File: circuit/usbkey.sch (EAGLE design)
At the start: 29 parts, among them IC1 ATmega168P, Q1 16MHz, X1 1503_09, X2 USB

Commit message: update
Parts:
- removed C5: 1u, resistor:C-US025-024X044
- removed C6: 0.1u, resistor:C-US025-024X044
- removed JP1: AVR-ISP-6VERT, avr-7:AVR-ISP-6VERT
- removed JP3: (no value), pinhead:PINHD-1X9
- removed R5: VARISTOR, varistor:VARISTOR-2,5
- removed R9: 1k, resistor:R-US_0204/7
- removed SPEAKER: (no value), pinhead:PINHD-1X2
- added D3, D4: 5V, diode:BZX55
- added P1: SPEAKER, pinhead:PINHD-1X2
- added PISP: AVR-ISP-6VERT, avr-7:AVR-ISP-6VERT
- C1, C2: value 0.1u -> 22p; device resistor:C-US025-024X044 -> c-j:C-50V-0302-2.54
- C3: device resistor:C-US025-024X044 -> c-j:C-50V-0302-2.54
- C4: value 1u -> 0.1u; device resistor:C-US025-024X044 -> c-j:C-50V-0302-2.54
- LED1: value (none) -> MONITOR
- P2: value (none) -> LED
- P3: value (none) -> OUTPUT
- R1, R2: value 168 -> 68; device resistor:R-US_0204/2V -> r-j:R-1/4W-07.62
- R3: device resistor:R-US_0204/7 -> r-j:R-1/4W-02.54-V
- R4: value VARISTOR -> 1.5k; device varistor:VARISTOR-2,5 -> r-j:R-1/4W-02.54-V
- R6: device resistor:R-US_0204/2V -> r-j:R-1/4W-02.54-V
- R7: device resistor:R-US_0204/2V -> r-j:R-1/4W-07.62
- R8: device resistor:R-US_0204/7 -> r-j:R-1/4W-07.62
- renumbered LED to P2, OUTPUT to P3
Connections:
- removed net N$20: C4.1, JP3.2
- removed net N$21: C5.1, JP3.4
- removed net N$22: C5.2, JP3.3
- removed net N$23: IC1.PC4(ADC4/SDA), JP3.7, R8.1
- removed net N$24: IC1.PC5(ADC5/SCL), JP3.8, R9.1
- net GND: now also C4.1, D3.A, D4.A, P1.2, PISP.6; no longer C6.2, JP1.6, JP3.6, R4.2, R5.2, SPEAKER.2
- net N$10: now also PISP.4; no longer JP1.4
- net N$11: now also PISP.3; no longer JP1.3
- net N$12: now also PISP.1; no longer JP1.1
- net N$14: now also P1.1; no longer SPEAKER.1
- net N$7: now also D3.C; no longer R4.1
- net N$8: now also D4.C; no longer R5.1
- net N$9: now also C4.2, PISP.5, R4.1; no longer JP1.5
- net VCC: now also IC1.AVCC, PISP.2, R4.2; no longer C4.2, C6.1, JP1.2, JP3.5, JP3.9, R8.2, R9.2
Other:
- moved on the sheet: SG1, X1

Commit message: update
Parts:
- removed R8: 1k, r-j:R-1/4W-07.62
- added C5, C6: 100p, c-j:C-50V-0302-2.54
- added JP1: (no value), pinhead:PINHD-1X3
- added JP2: (no value), pinhead:PINHD-1X6
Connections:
- new net N$20: IC1.PC0(ADC0), JP2.1
- new net N$21: IC1.PC1(ADC1), JP2.2
- new net N$22: IC1.PC2(ADC2), JP2.3
- new net N$23: IC1.PC3(ADC3), JP2.4
- new net N$24: IC1.PC4(ADC4/SDA), JP2.5
- new net N$25: IC1.PC5(ADC5/SCL), JP2.6
- net GND: now also C5.2, C6.2, JP1.1; no longer X1.1
- net N$3: now also C5.1
- net N$5: now also C6.1
- net N$7: now also JP1.3; no longer X1.3
- net N$8: now also JP1.2; no longer X1.2
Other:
- moved on the sheet: D3, D4, X1

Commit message: update
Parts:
- added C7: 0.1u, c-j:C-50V-0302-2.54
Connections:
- net GND: now also C7.1
- net VCC: now also C7.2
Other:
- moved on the sheet: LED1, OK1, P1, P2, P3, PISP, R6, R7, SG1

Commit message: update
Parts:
- R3: device r-j:R-1/4W-02.54-V -> r-j:R-1/4W-07.62
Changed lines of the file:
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@@
 <part name="R1" library="r-j" deviceset="R-" device="1/4W-07.62" value="68"/>
 <part name="R2" library="r-j" deviceset="R-" device="1/4W-07.62" value="68"/>
-<part name="R3" library="r-j" deviceset="R-" device="1/4W-02.54-V" value="1.5k"/>
+<part name="R3" library="r-j" deviceset="R-" device="1/4W-07.62" value="1.5k"/>
 <part name="GND3" library="supply1" deviceset="GND" device=""/>
 <part name="R6" library="r-j" deviceset="R-" device="1/4W-02.54-V" value="100"/>

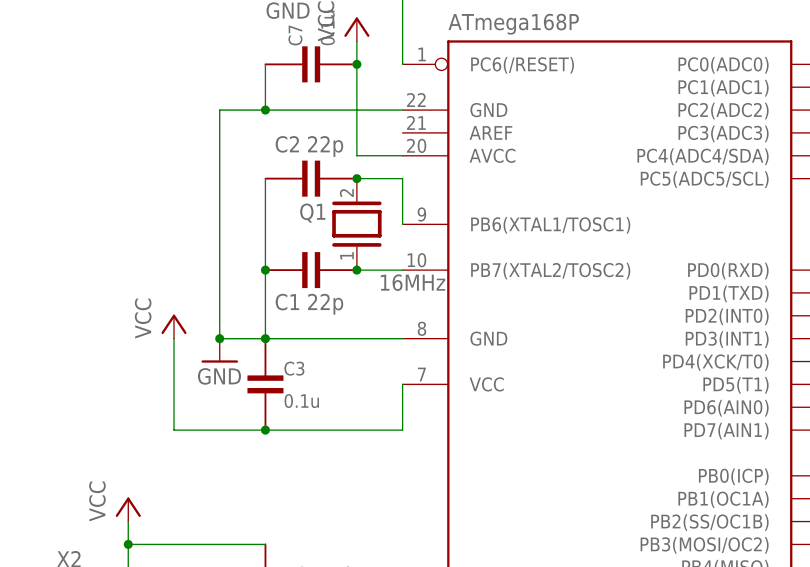
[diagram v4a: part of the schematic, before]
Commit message: F_CPU 18MHz
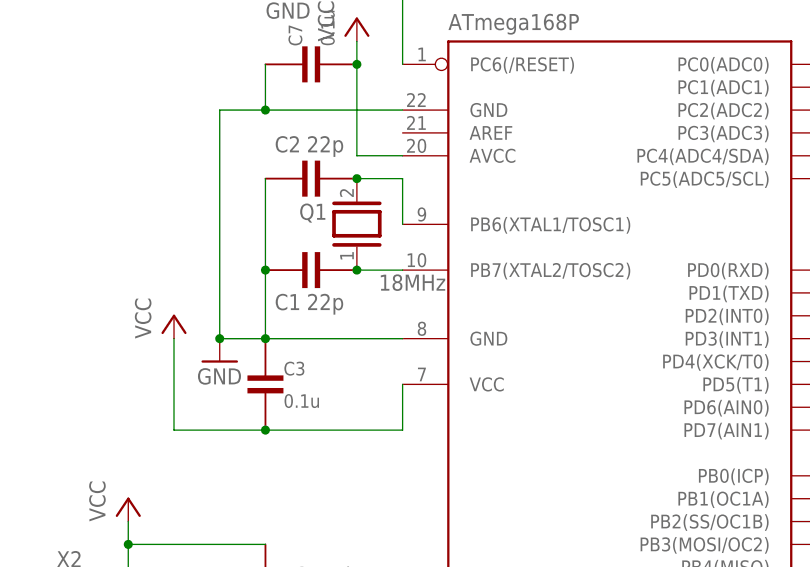
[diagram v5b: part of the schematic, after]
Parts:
- Q1: value 16MHz -> 18MHz
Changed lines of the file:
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@@
 <parts>
 <part name="IC1" library="atmel" deviceset="MEGA8-P" device="" value="ATmega168P"/>
-<part name="Q1" library="special" deviceset="XTAL/S" device="" value="16MHz"/>
+<part name="Q1" library="special" deviceset="XTAL/S" device="" value="18MHz"/>
 <part name="C1" library="c-j" deviceset="C-" device="50V-0302-2.54" value="22p"/>
 <part name="C2" library="c-j" deviceset="C-" device="50V-0302-2.54" value="22p"/>

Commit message: update
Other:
- moved on the sheet: C1, C2, C3, C5, C6, C7, D1, D2, D3, D4, JP1, Q1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

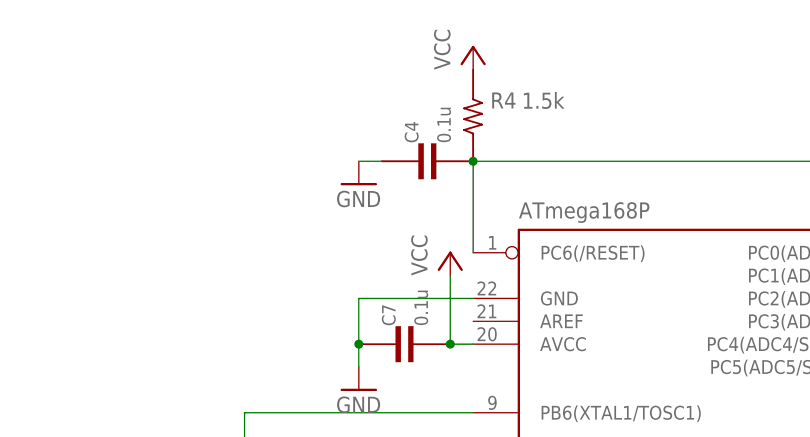
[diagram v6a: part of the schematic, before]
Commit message: reset の 0.1u は ISP ができなくなる
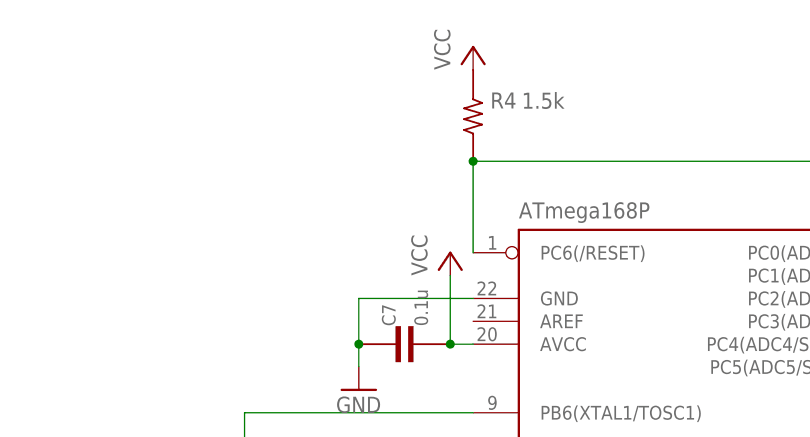
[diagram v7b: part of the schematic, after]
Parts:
- removed C4: 0.1u, c-j:C-50V-0302-2.54
- R1, R2: device r-j:R-1/4W-07.62 -> r-j:R-1/4W-02.54-V
- R6: device r-j:R-1/4W-02.54-V -> r-j:R-1/4W-07.62
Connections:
- net N$18 renamed OUT+
- net N$19 renamed OUT-
- net GND: no longer C4.1
- net N$9: no longer C4.2
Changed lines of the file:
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@@
 </variantdefs>
 <classes>
-<class number="0" name="default" width="0.8128" drill="0">
+<class number="0" name="default" width="0" drill="0">
 </class>
 </classes>
@@
 <part name="GND2" library="supply1" deviceset="GND" device=""/>
 <part name="P+2" library="supply1" deviceset="VCC" device=""/>
-<part name="R1" library="r-j" deviceset="R-" device="1/4W-07.62" value="68"/>
-<part name="R2" library="r-j" deviceset="R-" device="1/4W-07.62" value="68"/>
+<part name="R1" library="r-j" deviceset="R-" device="1/4W-02.54-V" value="68"/>
+<part name="R2" library="r-j" deviceset="R-" device="1/4W-02.54-V" value="68"/>
 <part name="R3" library="r-j" deviceset="R-" device="1/4W-07.62" value="1.5k"/>
 <part name="GND3" library="supply1" deviceset="GND" device=""/>
-<part name="R6" library="r-j" deviceset="R-" device="1/4W-02.54-V" value="100"/>
+<part name="R6" library="r-j" deviceset="R-" device="1/4W-07.62" value="100"/>
 <part name="R7" library="r-j" deviceset="R-" device="1/4W-07.62" value="1k"/>
 <part name="GND4" library="supply1" deviceset="GND" device=""/>
@@
 <part name="D3" library="diode" deviceset="BZX55" device="" value="5V"/>
 <part name="D4" library="diode" deviceset="BZX55" device="" value="5V"/>
-<part name="C4" library="c-j" deviceset="C-" device="50V-0302-2.54" value="0.1u"/>
-<part name="GND8" library="supply1" deviceset="GND" device=""/>
 <part name="R4" library="r-j" deviceset="R-" device="1/4W-02.54-V" value="1.5k"/>
 <part name="P+6" library="supply1" deviceset="VCC" device=""/>
@@
 <attribute name="VALUE" x="15.875" y="-28.448" size="1.778" layer="96" rot="R90"/>
 </instance>
-<instance part="C4" gate="C" x="27.94" y="99.06" rot="R90"/>
-<instance part="GND8" gate="1" x="20.32" y="96.52"/>
 <instance part="R4" gate="R" x="33.02" y="104.14" smashed="yes" rot="R90">
 <attribute name="NAME" x="37.846" y="106.7054" size="1.778" layer="95" rot="R180"/>
@@
 </segment>
 <segment>
-<pinref part="C4" gate="C" pin="1"/>
-<pinref part="GND8" gate="1" pin="GND"/>
-<wire x1="22.86" y1="99.06" x2="20.32" y2="99.06" width="0.1524" layer="91"/>
-</segment>
-<segment>
 <pinref part="C5" gate="C" pin="2"/>
 <pinref part="GND6" gate="1" pin="GND"/>
@@
 <pinref part="IC1" gate="G$1" pin="PC6(/RESET)"/>
 <wire x1="33.02" y1="99.06" x2="33.02" y2="88.9" width="0.1524" layer="91"/>
-<pinref part="C4" gate="C" pin="2"/>
 <junction x="33.02" y="99.06"/>
 <pinref part="R4" gate="R" pin="1"/>
@@
 </segment>
 </net>
-<net name="N$18" class="0">
+<net name="OUT+" class="0">
 <segment>
 <pinref part="OK1" gate="G$1" pin="COL"/>
@@
 </segment>
 </net>
-<net name="N$19" class="0">
+<net name="OUT-" class="0">
 <segment>
 <pinref part="P3" gate="G$1" pin="2"/>

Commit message: update
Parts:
- removed JP2: (no value), pinhead:PINHD-1X6
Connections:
- removed net N$20: IC1.PC0(ADC0), JP2.1
- removed net N$21: IC1.PC1(ADC1), JP2.2
- removed net N$22: IC1.PC2(ADC2), JP2.3
- removed net N$23: IC1.PC3(ADC3), JP2.4
- removed net N$24: IC1.PC4(ADC4/SDA), JP2.5
- removed net N$25: IC1.PC5(ADC5/SCL), JP2.6
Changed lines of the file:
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@@
 <part name="GND6" library="supply1" deviceset="GND" device=""/>
 <part name="JP1" library="pinhead" deviceset="PINHD-1X3" device=""/>
-<part name="JP2" library="pinhead" deviceset="PINHD-1X6" device=""/>
 <part name="C7" library="c-j" deviceset="C-" device="50V-0302-2.54" value="0.1u"/>
 <part name="GND9" library="supply1" deviceset="GND" device=""/>
@@
 <instance part="GND6" gate="1" x="73.66" y="-12.7"/>
 <instance part="JP1" gate="A" x="-7.62" y="-22.86" rot="R180"/>
-<instance part="JP2" gate="A" x="139.7" y="81.28"/>
 <instance part="C7" gate="C" x="25.4" y="78.74" rot="R90"/>
 <instance part="GND9" gate="1" x="30.48" y="27.94"/>
@@
 </segment>
 </net>
-<net name="N$20" class="0">
-<segment>
-<pinref part="JP2" gate="A" pin="1"/>
-<pinref part="IC1" gate="G$1" pin="PC0(ADC0)"/>
-<wire x1="137.16" y1="88.9" x2="81.28" y2="88.9" width="0.1524" layer="91"/>
-</segment>
-</net>
-<net name="N$21" class="0">
-<segment>
-<pinref part="JP2" gate="A" pin="2"/>
-<pinref part="IC1" gate="G$1" pin="PC1(ADC1)"/>
-<wire x1="137.16" y1="86.36" x2="81.28" y2="86.36" width="0.1524" layer="91"/>
-</segment>
-</net>
-<net name="N$22" class="0">
-<segment>
-<pinref part="JP2" gate="A" pin="3"/>
-<pinref part="IC1" gate="G$1" pin="PC2(ADC2)"/>
-<wire x1="137.16" y1="83.82" x2="81.28" y2="83.82" width="0.1524" layer="91"/>
-</segment>
-</net>
-<net name="N$23" class="0">
-<segment>
-<pinref part="JP2" gate="A" pin="4"/>
-<pinref part="IC1" gate="G$1" pin="PC3(ADC3)"/>
-<wire x1="137.16" y1="81.28" x2="81.28" y2="81.28" width="0.1524" layer="91"/>
-</segment>
-</net>
-<net name="N$24" class="0">
-<segment>
-<pinref part="JP2" gate="A" pin="5"/>
-<pinref part="IC1" gate="G$1" pin="PC4(ADC4/SDA)"/>
-<wire x1="137.16" y1="78.74" x2="81.28" y2="78.74" width="0.1524" layer="91"/>
-</segment>
-</net>
-<net name="N$25" class="0">
-<segment>
-<pinref part="JP2" gate="A" pin="6"/>
-<pinref part="IC1" gate="G$1" pin="PC5(ADC5/SCL)"/>
-<wire x1="137.16" y1="76.2" x2="81.28" y2="76.2" width="0.1524" layer="91"/>
-</segment>
-</net>
